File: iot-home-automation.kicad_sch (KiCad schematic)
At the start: 32 parts, among them J1 Conn_01x16_Female, J2 USB_C_Receptacle_USB2.0_16P, J3 440055-2, J5 Conn_01x02_Pin, J6 Conn_01x08_Pin, SW2 SW_Push, SW3 SW_Push, U2 SHTC3, U3 453-00059R, U4 NPM1300-QEAA-R7

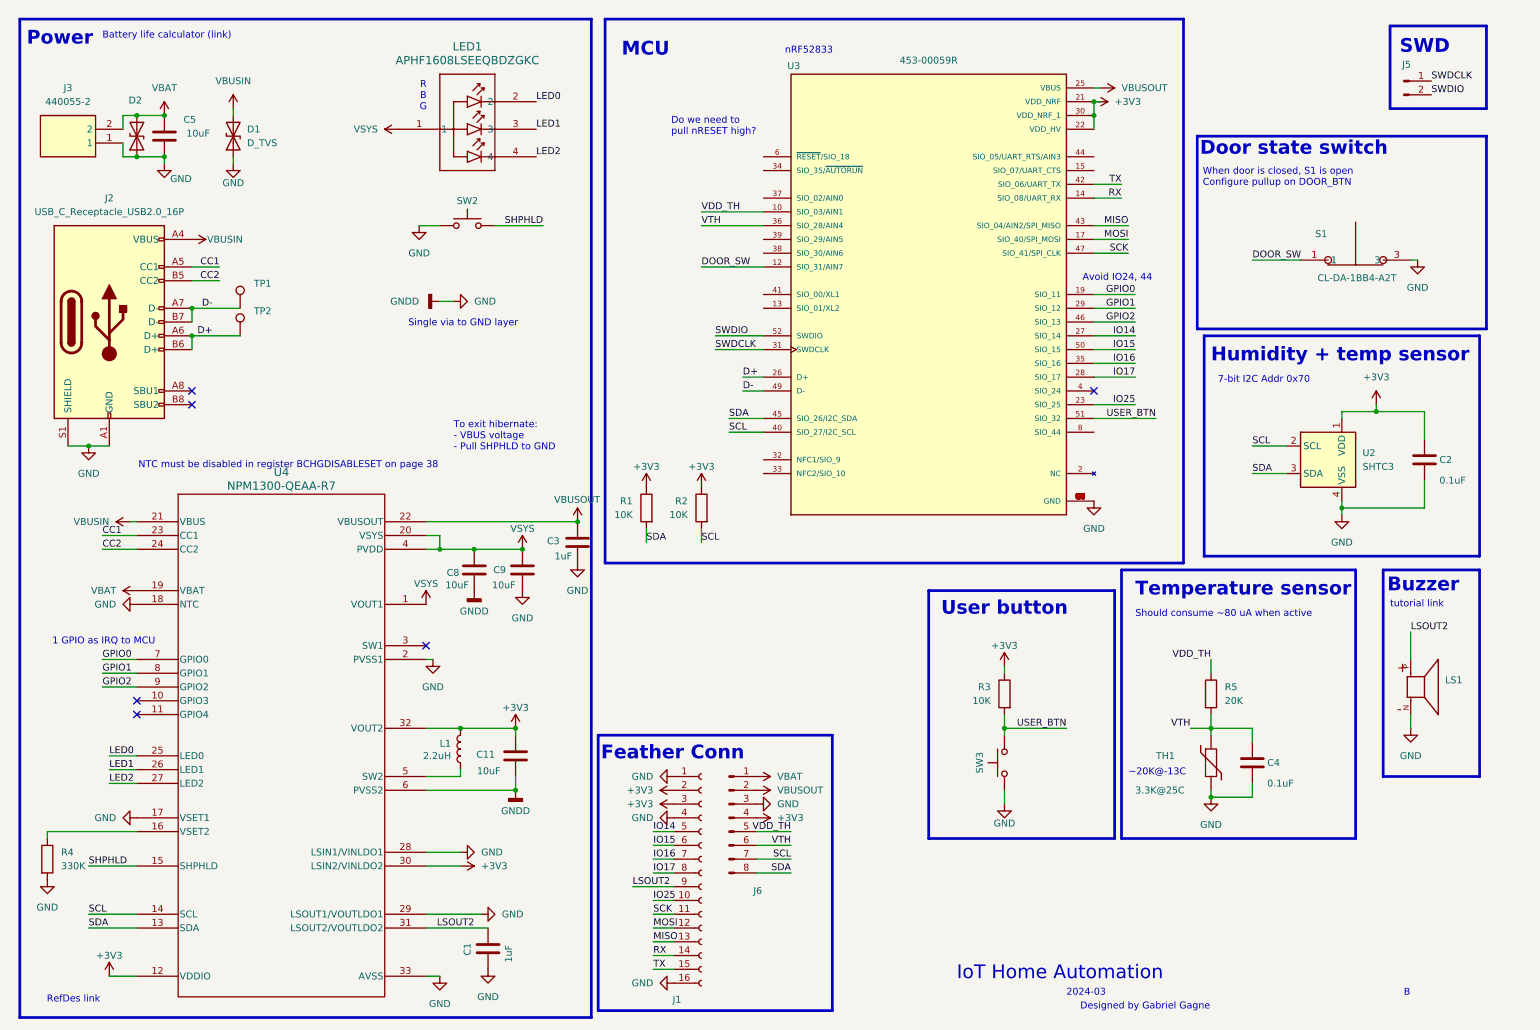
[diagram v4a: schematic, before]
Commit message: add 3d models
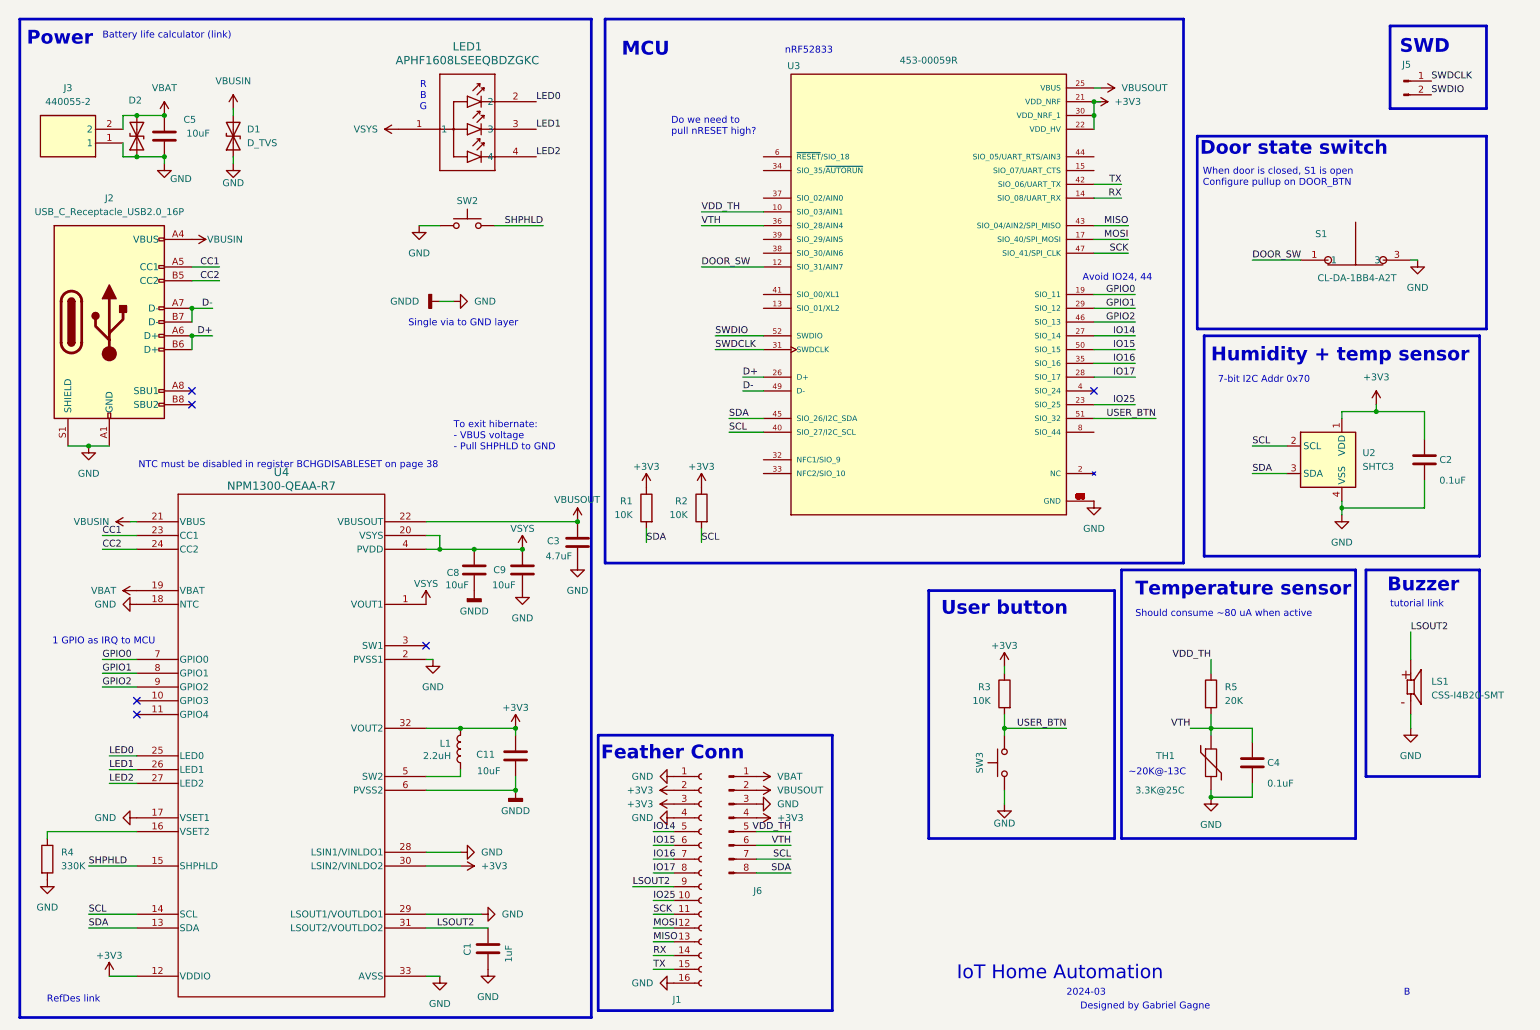
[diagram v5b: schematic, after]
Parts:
- removed LS1: AI-1223-TWT-3V-2-R, AI-1223-TWT-3V-2-R:XDCR_AI-1223-TWT-3V-2-R, symbol AI-1223-TWT-3V-2-R:AI-1223-TWT-3V-2-R
- removed TP1, TP2: TestPoint, TestPoint:TestPoint_Pad_D1.5mm, symbol Connector:TestPoint
- added LS1: CSS-I4B20-SMT, CUI_CSS-I4B20-SMT, symbol CSS-I4B20-SMT:CSS-I4B20-SMT
- C3: value 1uF -> 4.7uF
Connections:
- net GND: now also LS1.M1, LS1.M2
- net LSOUT2: now also LS1.P1, LS1.P2
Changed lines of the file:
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@@
 	)
 	(rectangle
-		(start 265.43 115.57)
+		(start 262.255 115.57)
 		(end 283.21 153.67)
 		(stroke
@@
 	)
 	(junction
-		(at 45.72 67.31)
+		(at 116.84 106.68)
 		(diameter 0)
 		(color 0 0 0 0)
 	)
 	(junction
-		(at 116.84 106.68)
+		(at 212.09 29.21)
 		(diameter 0)
 		(color 0 0 0 0)
 	)
 	(junction
-		(at 212.09 29.21)
+		(at 45.72 67.31)
 		(diameter 0)
 		(color 0 0 0 0)
 	)
 	(junction
-		(at 212.09 31.75)
+		(at 45.72 72.39)
 		(diameter 0)
 		(color 0 0 0 0)
 	)
 	(junction
-		(at 35.56 39.37)
+		(at 212.09 31.75)
 		(diameter 0)
 		(color 0 0 0 0)
 	)
 	(junction
-		(at 257.81 104.14)
+		(at 35.56 39.37)
 		(diameter 0)
 		(color 0 0 0 0)
 	)
 	(junction
-		(at 40.64 39.37)
+		(at 257.81 104.14)
 		(diameter 0)
 		(color 0 0 0 0)
 	)
 	(junction
-		(at 45.72 72.39)
+		(at 40.64 39.37)
 		(diameter 0)
 		(color 0 0 0 0)
@@
 	(wire
 		(pts
-			(xy 195.58 144.78) (xy 207.01 144.78)
-		)
-		(stroke
-			(width 0)
-			(type default)
-		)
-	)
-	(wire
-		(pts
 			(xy 212.09 80.01) (xy 219.71 80.01)
 		)
@@
 	(wire
 		(pts
-			(xy 45.72 72.39) (xy 54.61 72.39)
+			(xy 195.58 144.78) (xy 195.58 142.24)
 		)
 		(stroke
@@
 	(wire
 		(pts
-			(xy 195.58 144.78) (xy 195.58 142.24)
+			(xy 105.41 144.78) (xy 105.41 146.05)
 		)
 		(stroke
@@
 	(wire
 		(pts
-			(xy 105.41 144.78) (xy 105.41 146.05)
+			(xy 195.58 144.78) (xy 207.01 144.78)
 		)
 		(stroke
@@
 	(wire
 		(pts
+			(xy 45.72 72.39) (xy 49.53 72.39)
+		)
+		(stroke
+			(width 0)
+			(type default)
+		)
+	)
+	(wire
+		(pts
 			(xy 144.78 87.63) (xy 151.13 87.63)
 		)
@@
 	(wire
 		(pts
-			(xy 45.72 67.31) (xy 54.61 67.31)
+			(xy 45.72 67.31) (xy 49.53 67.31)
 		)
 		(stroke
@@
 	)
 	(symbol
-		(lib_id "Connector:TestPoint")
-		(at 54.61 67.31 0)
-		(unit 1)
-		(exclude_from_sim no)
-		(in_bom yes)
-		(on_board yes)
-		(dnp no)
-		(fields_autoplaced yes)
-		(property "Reference" "TP1"
-			(at 57.15 62.7379 0)
-			(effects
-				(font
-					(size 1.27 1.27)
-				)
-				(justify left)
-			)
-		)
-		(property "Value" "TestPoint"
-			(at 57.15 65.2779 0)
-			(effects
-				(font
-					(size 1.27 1.27)
-				)
-				(justify left)
-				(hide yes)
-			)
-		)
-		(property "Footprint" "TestPoint:TestPoint_Pad_D1.5mm"
-			(at 59.69 67.31 0)
-			(effects
-				(font
-					(size 1.27 1.27)
-				)
-				(hide yes)
-			)
-		)
-		(property "Datasheet" "~"
-			(at 59.69 67.31 0)
-			(effects
-				(font
-					(size 1.27 1.27)
-				)
-				(hide yes)
-			)
-		)
-		(property "Description" "test point"
-			(at 54.61 67.31 0)
-			(effects
-				(font
-					(size 1.27 1.27)
-				)
-				(hide yes)
-			)
-		)
-		(pin "1"
-		)
-		(instances
-			(project ""
-				(path "/f972dc2a-b689-48e4-bca2-667a07f35e11"
-					(reference "TP1")
-					(unit 1)
-				)
-			)
-		)
-	)
-	(symbol
 		(lib_id "Device:C")
 		(at 273.05 95.25 0)
@@
 	)
 	(symbol
-		(lib_id "Connector:TestPoint")
-		(at 54.61 72.39 0)
-		(unit 1)
-		(exclude_from_sim no)
-		(in_bom yes)
-		(on_board yes)
-		(dnp no)
-		(fields_autoplaced yes)
-		(property "Reference" "TP2"
-			(at 57.15 67.8179 0)
-			(effects
-				(font
-					(size 1.27 1.27)
-				)
-				(justify left)
-			)
-		)
-		(property "Value" "TestPoint"
-			(at 57.15 70.3579 0)
-			(effects
-				(font
-					(size 1.27 1.27)
-				)
-				(justify left)
-				(hide yes)
-			)
-		)
-		(property "Footprint" "TestPoint:TestPoint_Pad_D1.5mm"
-			(at 59.69 72.39 0)
-			(effects
-				(font
-					(size 1.27 1.27)
-				)
-				(hide yes)
-			)
-		)
-		(property "Datasheet" "~"
-			(at 59.69 72.39 0)
-			(effects
-				(font
-					(size 1.27 1.27)
-				)
-				(hide yes)
-			)
-		)
-		(property "Description" "test point"
-			(at 54.61 72.39 0)
-			(effects
-				(font
-					(size 1.27 1.27)
-				)
-				(hide yes)
-			)
-		)
-		(pin "1"
-		)
-		(instances
-			(project "iot-home-automation"
-				(path "/f972dc2a-b689-48e4-bca2-667a07f35e11"
-					(reference "TP2")
-					(unit 1)
-				)
-			)
-		)
-	)
-	(symbol
 		(lib_id "Device:C")
 		(at 106.68 115.57 0)
@@
 	)
 	(symbol
+		(lib_id "CSS-I4B20-SMT:CSS-I4B20-SMT")
+		(at 270.51 137.16 0)
+		(unit 1)
+		(exclude_from_sim no)
+		(in_bom yes)
+		(on_board yes)
+		(dnp no)
+		(fields_autoplaced yes)
+		(property "Reference" "LS1"
+			(at 274.32 136.1452 0)
+			(effects
+				(font
+					(size 1.27 1.27)
+				)
+				(justify left)
+			)
+		)
+		(property "Value" "CSS-I4B20-SMT"
+			(at 274.32 138.6852 0)
+			(effects
+				(font
+					(size 1.27 1.27)
+				)
+				(justify left)
+			)
+		)
+		(property "Footprint" "CUI_CSS-I4B20-SMT"
+			(at 270.51 137.16 0)
+			(effects
+				(font
+					(size 1.27 1.27)
+				)
+				(justify left bottom)
+				(hide yes)
+			)
+		)
+		(property "Datasheet" "https://www.digikey.ca/en/products/detail/same-sky-formerly-cui-devices/CSS-I4B20-SMT-TR/1003796?s=N4IgTCBcDaIMIGUEFoCSAWAQmADMhAsgCogC6AvkA"
+			(at 270.51 137.16 0)
+			(effects
+				(font
+					(size 1.27 1.27)
+				)
+				(justify left bottom)
+				(hide yes)
+			)
+		)
+		(property "Description" ""
+			(at 270.51 137.16 0)
+			(effects
+				(font
+					(size 1.27 1.27)
+				)
+				(hide yes)
+			)
+		)
+		(property "MF" "CUI"
+			(at 270.51 137.16 0)
+			(effects
+				(font
+					(size 1.27 1.27)
+				)
+				(justify left bottom)
+				(hide yes)
+			)
+		)
+		(property "DESCRIPTION" "8.5 mm, 3.6 V, 85 dB, Surface Mount _SMT_, Magnetic Audio Transducer Buzzer"
+			(at 270.51 137.16 0)
+			(effects
+				(font
+					(size 1.27 1.27)
+				)
+				(justify left bottom)
+				(hide yes)
+			)
+		)
+		(property "PACKAGE" "None"
+			(at 270.51 137.16 0)
+			(effects
+				(font
+					(size 1.27 1.27)
+				)
+				(justify left bottom)
+				(hide yes)
+			)
+		)
+		(property "PRICE" "None"
+			(at 270.51 137.16 0)
+			(effects
+				(font
+					(size 1.27 1.27)
+				)
+				(justify left bottom)
+				(hide yes)
+			)
+		)
+		(property "MP" "CSS-I4B20-SMT"
+			(at 270.51 137.16 0)
+			(effects
+				(font
+					(size 1.27 1.27)
+				)
+				(justify left bottom)
+				(hide yes)
+			)
+		)
+		(property "AVAILABILITY" "Unavailable"
+			(at 270.51 137.16 0)
+			(effects
+				(font
+					(size 1.27 1.27)
+				)
+				(justify left bottom)
+				(hide yes)
+			)
+		)
+		(pin "M2"
+		)
+		(pin "M1"
+		)
+		(pin "P1"
+		)
+		(pin "P2"
+		)
+		(instances
+			(project ""
+				(path "/f972dc2a-b689-48e4-bca2-667a07f35e11"
+					(reference "LS1")
+					(unit 1)
+				)
+			)
+		)
+	)
+	(symbol
 		(lib_id "power:GND")
 		(at 257.81 105.41 0)
@@
 			)
 		)
-		(property "Value" "1uF"
+		(property "Value" "4.7uF"
 			(at 115.824 113.03 0)
 			(effects
@@
 					(unit 1)
 				)
-			)
-		)
-	)
-	(symbol
-		(lib_id "AI-1223-TWT-3V-2-R:AI-1223-TWT-3V-2-R")
-		(at 273.05 137.16 0)
-		(unit 1)
-		(exclude_from_sim no)
-		(in_bom yes)
-		(on_board yes)
-		(dnp no)
-		(property "Reference" "LS1"
-			(at 276.86 135.89 0)
-			(effects
-				(font
-					(size 1.27 1.27)
-				)
-				(justify left)
-			)
-		)
-		(property "Value" "AI-1223-TWT-3V-2-R"
-			(at 265.43 148.59 90)
-			(effects
-				(font
-					(size 1.27 1.27)
-				)
-				(justify left)
-				(hide yes)
-			)
-		)
-		(property "Footprint" "AI-1223-TWT-3V-2-R:XDCR_AI-1223-TWT-3V-2-R"
-			(at 273.05 137.16 0)
-			(effects
-				(font
-					(size 1.27 1.27)
-				)
-				(justify bottom)
-				(hide yes)
-			)
-		)
-		(property "Datasheet" ""
-			(at 273.05 137.16 0)
-			(effects
-				(font
-					(size 1.27 1.27)
-				)
-				(hide yes)
-			)
-		)
-		(property "Description" ""
-			(at 273.05 137.16 0)
-			(effects
-				(font
-					(size 1.27 1.27)
-				)
-				(hide yes)
-			)
-		)
-		(property "Link" "https://www.digikey.ca/en/products/detail/pui-audio-inc/AI-1223-TWT-3V-2-R/5011391"
-			(at 273.05 137.16 0)
-			(effects
-				(font
-					(size 1.27 1.27)
-				)
-				(hide yes)
-			)
-		)
-		(pin "N"
-		)
-		(pin "P"
-		)
-		(instances
-			(project "iot-home-automation"
-				(path "/f972dc2a-b689-48e4-bca2-667a07f35e11"
-					(reference "LS1")
-					(unit 1)
-				)
